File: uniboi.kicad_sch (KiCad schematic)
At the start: 0 parts

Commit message: WIP: first draft of schematics
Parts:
- added C1: 4.7uF, symbol Device:C
- added C2, C3: 0.1uF, symbol Device:C
- added C4, C6, C7: 1uF, symbol Device:C
- added C5: C, symbol Device:C
- added F1: 1A, symbol Device:Polyfuse
- added J1: USB_C_Receptacle_USB2.0_16P, symbol Connector:USB_C_Receptacle_USB2.0_16P
- added R1: 10k, symbol Device:R
- added R2, R3: 5.1k, symbol Device:R
- added SW1: SW_Push, symbol Switch:SW_Push
- added SW2: SW_SPDT, symbol Switch:SW_SPDT
- added U1: STM32G0B1CBTx, Package_QFP:LQFP-48_7x7mm_P0.5mm, symbol MCU_ST_STM32G0:STM32G0B1CBTx
- added U2: SRV05-4, Package_TO_SOT_SMD:SOT-23-6, symbol Power_Protection:SRV05-4
- added U3: XC6206P332MR, Package_TO_SOT_SMD:SOT-23-3, symbol Regulator_Linear:XC6206PxxxMR
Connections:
- new net: J1.B5 (CC2), R2.1
- new net: R1.2, SW2.2 (B)
- new net: J1.A5 (CC1), R3.1
- new net +3.3V: C1.1, C2.1, C3.1, C4.1, C7.1, SW2.3 (C), U1.4 (VBAT), U1.5 (VREF+), U1.6 (VDD), U3.2 (VO)
- new net +5V: C6.1, F1.2, U2.5 (VP), U3.3 (VI)
- new net BOOT0: R1.1, U1.36 (PA14)
- new net D+: J1.A6 (D+), J1.B6 (D+), U1.34 (PA10/PA12)
- new net D-: J1.A7 (D-), J1.B7 (D-), U1.33 (PA9/PA11)
- new net GND: C1.2, C2.2, C3.2, C4.2, C5.2, C6.2, C7.2, J1.A1 (GND), J1.A12 (GND), J1.B1 (GND), J1.B12 (GND), J1.S1 (SHIELD), R2.2, R3.2, SW1.2, SW2.1 (A), U1.7 (VSS), U2.2 (VN), U3.1 (GND)
- new net VBUS: F1.1, J1.A4 (VBUS), J1.A9 (VBUS), J1.B4 (VBUS), J1.B9 (VBUS)
- new net nRST: C5.1, SW1.1, U1.10 (PF2)
- no-connect marks 0 -> 2
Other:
- added sheet matrix (matrix.kicad_sch)

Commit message: added keyswitch footprint submodule
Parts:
- C1, C2, C3, C4, C5, C6, C7: footprint (none) -> Capacitor_SMD:C_0805_2012Metric
- F1: footprint (none) -> Fuse:Fuse_1206_3216Metric
- J1: footprint (none) -> Connector_USB:USB_C_Receptacle_HRO_TYPE-C-31-M-12
- R1, R2, R3: footprint (none) -> Resistor_SMD:R_0805_2012Metric
- SW1: footprint (none) -> Button_Switch_SMD:SW_SPST_TS-1088-xR020
- SW2: footprint (none) -> Button_Switch_SMD:SW_SPDT_PCM12
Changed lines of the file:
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@@
 			)
 		)
-		(property "Footprint" ""
+		(property "Footprint" "Capacitor_SMD:C_0805_2012Metric"
 			(at 350.2152 134.62 0)
 			(effects
@@
 			)
 		)
-		(property "Footprint" ""
+		(property "Footprint" "Resistor_SMD:R_0805_2012Metric"
 			(at 66.802 45.72 90)
 			(effects
@@
 			)
 		)
-		(property "Footprint" ""
+		(property "Footprint" "Capacitor_SMD:C_0805_2012Metric"
 			(at 195.2752 88.9 0)
 			(effects
@@
 			)
 		)
-		(property "Footprint" ""
+		(property "Footprint" "Capacitor_SMD:C_0805_2012Metric"
 			(at 180.0352 88.9 0)
 			(effects
@@
 			)
 		)
-		(property "Footprint" ""
+		(property "Footprint" "Button_Switch_SMD:SW_SPST_TS-1088-xR020"
 			(at 370.84 130.81 0)
 			(effects
@@
 			)
 		)
-		(property "Footprint" ""
+		(property "Footprint" "Button_Switch_SMD:SW_SPDT_PCM12"
 			(at 370.84 157.48 0)
 			(effects
@@
 			)
 		)
-		(property "Footprint" ""
+		(property "Footprint" "Capacitor_SMD:C_0805_2012Metric"
 			(at 237.1852 83.82 0)
 			(effects
@@
 			)
 		)
-		(property "Footprint" ""
+		(property "Footprint" "Resistor_SMD:R_0805_2012Metric"
 			(at 359.41 159.258 90)
 			(effects
@@
 			)
 		)
-		(property "Footprint" ""
+		(property "Footprint" "Connector_USB:USB_C_Receptacle_HRO_TYPE-C-31-M-12"
 			(at 36.83 48.26 0)
 			(effects
@@
 			)
 		)
-		(property "Footprint" ""
+		(property "Footprint" "Capacitor_SMD:C_0805_2012Metric"
 			(at 129.2352 45.72 0)
 			(effects
@@
 			)
 		)
-		(property "Footprint" ""
+		(property "Footprint" "Capacitor_SMD:C_0805_2012Metric"
 			(at 101.2952 45.72 0)
 			(effects
@@
 			)
 		)
-		(property "Footprint" ""
+		(property "Footprint" "Fuse:Fuse_1206_3216Metric"
 			(at 72.39 31.75 0)
 			(effects
@@
 			)
 		)
-		(property "Footprint" ""
+		(property "Footprint" "Capacitor_SMD:C_0805_2012Metric"
 			(at 249.8852 83.82 0)
 			(effects
@@
 			)
 		)
-		(property "Footprint" ""
+		(property "Footprint" "Resistor_SMD:R_0805_2012Metric"
 			(at 75.692 45.72 90)
 			(effects

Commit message: WIP:routing
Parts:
- C1, C2, C3, C4, C6, C7: footprint Capacitor_SMD:C_0805_2012Metric -> Capacitor_SMD:C_0402_1005Metric
- C5: value C -> 0.1uF; footprint Capacitor_SMD:C_0805_2012Metric -> Capacitor_SMD:C_0402_1005Metric
- R1, R2, R3: footprint Resistor_SMD:R_0805_2012Metric -> Resistor_SMD:R_0402_1005Metric
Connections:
- net COL1: now reaches U1.47 (PB8)
- net COL0: now reaches U1.48 (PB9)
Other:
- sheet matrix ports: added COL0, COL1, ROW0, ROW1; removed none
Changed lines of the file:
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@@
+		)
+	)
+	(global_label "COL1"
+		(shape input)
+		(at 151.13 123.19 0)
+		(fields_autoplaced yes)
+		(effects
+			(font
+				(size 1.27 1.27)
+			)
+			(justify left)
+		)
+		(property "Intersheetrefs" "${INTERSHEET_REFS}"
+			(at 158.9533 123.19 0)
+			(effects
+				(font
+					(size 1.27 1.27)
+				)
+				(justify left)
+				(hide yes)
+			)
 		)
 	)
@@
 		)
 	)
+	(global_label "COL0"
+		(shape input)
+		(at 151.13 119.38 0)
+		(fields_autoplaced yes)
+		(effects
+			(font
+				(size 1.27 1.27)
+			)
+			(justify left)
+		)
+		(property "Intersheetrefs" "${INTERSHEET_REFS}"
+			(at 158.9533 119.38 0)
+			(effects
+				(font
+					(size 1.27 1.27)
+				)
+				(justify left)
+				(hide yes)
+			)
+		)
+	)
 	(global_label "D+"
 		(shape input)
@@
 		)
 	)
+	(global_label "COL0"
+		(shape input)
+		(at 252.73 163.83 0)
+		(fields_autoplaced yes)
+		(effects
+			(font
+				(size 1.27 1.27)
+			)
+			(justify left)
+		)
+		(property "Intersheetrefs" "${INTERSHEET_REFS}"
+			(at 260.5533 163.83 0)
+			(effects
+				(font
+					(size 1.27 1.27)
+				)
+				(justify left)
+				(hide yes)
+			)
+		)
+	)
+	(global_label "COL1"
+		(shape input)
+		(at 252.73 161.29 0)
+		(fields_autoplaced yes)
+		(effects
+			(font
+				(size 1.27 1.27)
+			)
+			(justify left)
+		)
+		(property "Intersheetrefs" "${INTERSHEET_REFS}"
+			(at 260.5533 161.29 0)
+			(effects
+				(font
+					(size 1.27 1.27)
+				)
+				(justify left)
+				(hide yes)
+			)
+		)
+	)
 	(global_label "D-"
 		(shape input)
@@
 			)
 		)
-		(property "Value" "C"
+		(property "Value" "0.1uF"
 			(at 353.06 132.0799 0)
 			(effects
@@
 			)
 		)
-		(property "Footprint" "Capacitor_SMD:C_0805_2012Metric"
+		(property "Footprint" "Capacitor_SMD:C_0402_1005Metric"
 			(at 350.2152 134.62 0)
 			(effects
@@
 			)
 		)
-		(property "Footprint" "Resistor_SMD:R_0805_2012Metric"
+		(property "Footprint" "Resistor_SMD:R_0402_1005Metric"
 			(at 66.802 45.72 90)
 			(effects
@@
 			)
 		)
-		(property "Footprint" "Capacitor_SMD:C_0805_2012Metric"
+		(property "Footprint" "Capacitor_SMD:C_0402_1005Metric"
 			(at 195.2752 88.9 0)
 			(effects
@@
 			)
 		)
-		(property "Footprint" "Capacitor_SMD:C_0805_2012Metric"
+		(property "Footprint" "Capacitor_SMD:C_0402_1005Metric"
 			(at 180.0352 88.9 0)
 			(effects
@@
 			)
 		)
-		(property "Footprint" "Capacitor_SMD:C_0805_2012Metric"
+		(property "Footprint" "Capacitor_SMD:C_0402_1005Metric"
 			(at 237.1852 83.82 0)
 			(effects
@@
 			)
 		)
-		(property "Footprint" "Resistor_SMD:R_0805_2012Metric"
+		(property "Footprint" "Resistor_SMD:R_0402_1005Metric"
 			(at 359.41 159.258 90)
 			(effects
@@
 			)
 		)
-		(property "Footprint" "Capacitor_SMD:C_0805_2012Metric"
+		(property "Footprint" "Capacitor_SMD:C_0402_1005Metric"
 			(at 129.2352 45.72 0)
 			(effects
@@
 			)
 		)
-		(property "Footprint" "Capacitor_SMD:C_0805_2012Metric"
+		(property "Footprint" "Capacitor_SMD:C_0402_1005Metric"
 			(at 101.2952 45.72 0)
 			(effects
@@
 			)
 		)
-		(property "Footprint" "Capacitor_SMD:C_0805_2012Metric"
+		(property "Footprint" "Capacitor_SMD:C_0402_1005Metric"
 			(at 249.8852 83.82 0)
 			(effects
@@
 			)
 		)
-		(property "Footprint" "Resistor_SMD:R_0805_2012Metric"
+		(property "Footprint" "Resistor_SMD:R_0402_1005Metric"
 			(at 75.692 45.72 90)
 			(effects
@@
 	)
 	(sheet
-		(at 53.34 114.3)
-		(size 104.14 118.11)
+		(at 115.57 104.14)
+		(size 35.56 50.8)
 		(exclude_from_sim no)
 		(in_bom yes)
@@
 		)
 		(property "Sheetname" "matrix"
-			(at 53.34 113.5884 0)
+			(at 115.57 103.4284 0)
 			(effects
 				(font
@@
 		)
 		(property "Sheetfile" "matrix.kicad_sch"
-			(at 53.34 232.9946 0)
+			(at 115.57 155.5246 0)
 			(effects
 				(font
@@
 			)
 		)
+		(pin "COL1" input
+			(at 151.13 123.19 0)
+			(effects
+				(font
+					(size 1.27 1.27)
+				)
+				(justify right)
+			)
+		)
+		(pin "ROW1" input
+			(at 151.13 147.32 0)
+			(effects
+				(font
+					(size 1.27 1.27)
+				)
+				(justify right)
+			)
+		)
+		(pin "COL0" input
+			(at 151.13 119.38 0)
+			(effects
+				(font
+					(size 1.27 1.27)
+				)
+				(justify right)
+			)
+		)
+		(pin "ROW0" input
+			(at 151.13 143.51 0)
+			(effects
+				(font
+					(size 1.27 1.27)
+				)
+				(justify right)
+			)
+		)

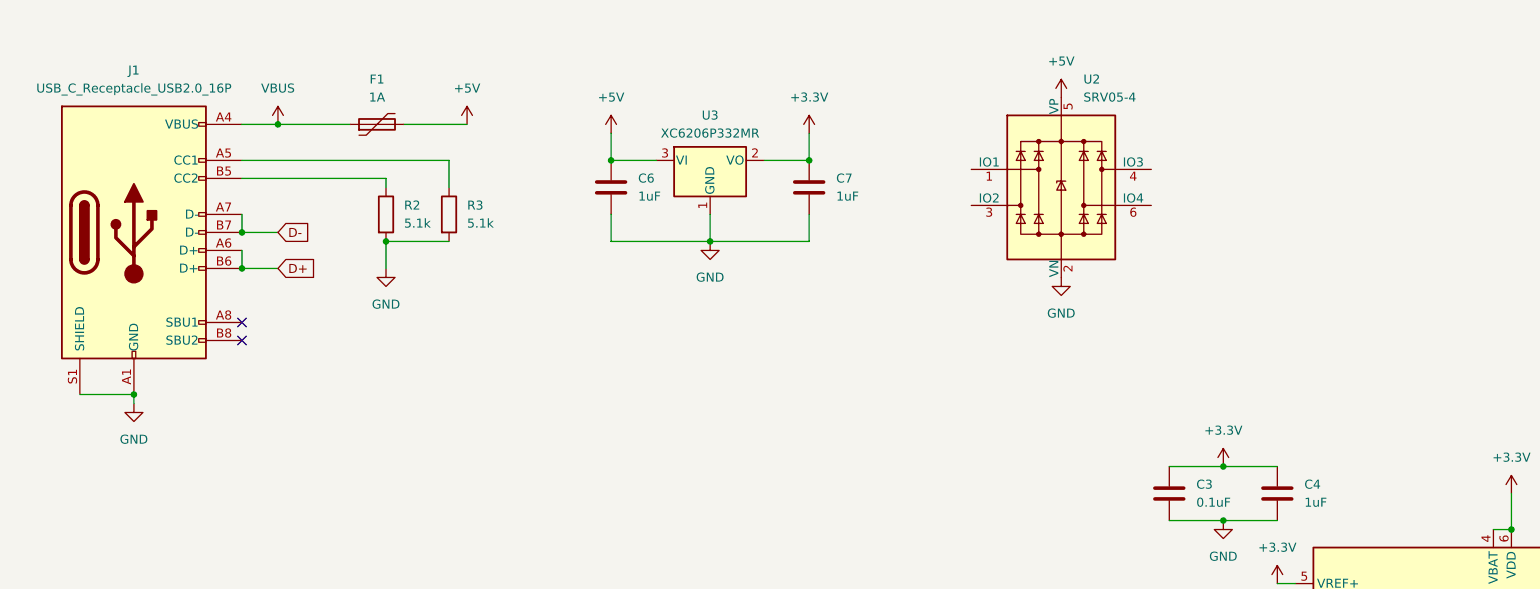
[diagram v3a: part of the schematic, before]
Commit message: WIP: changed usb-c connector, updated schematics with the SRV05-4, updated routing
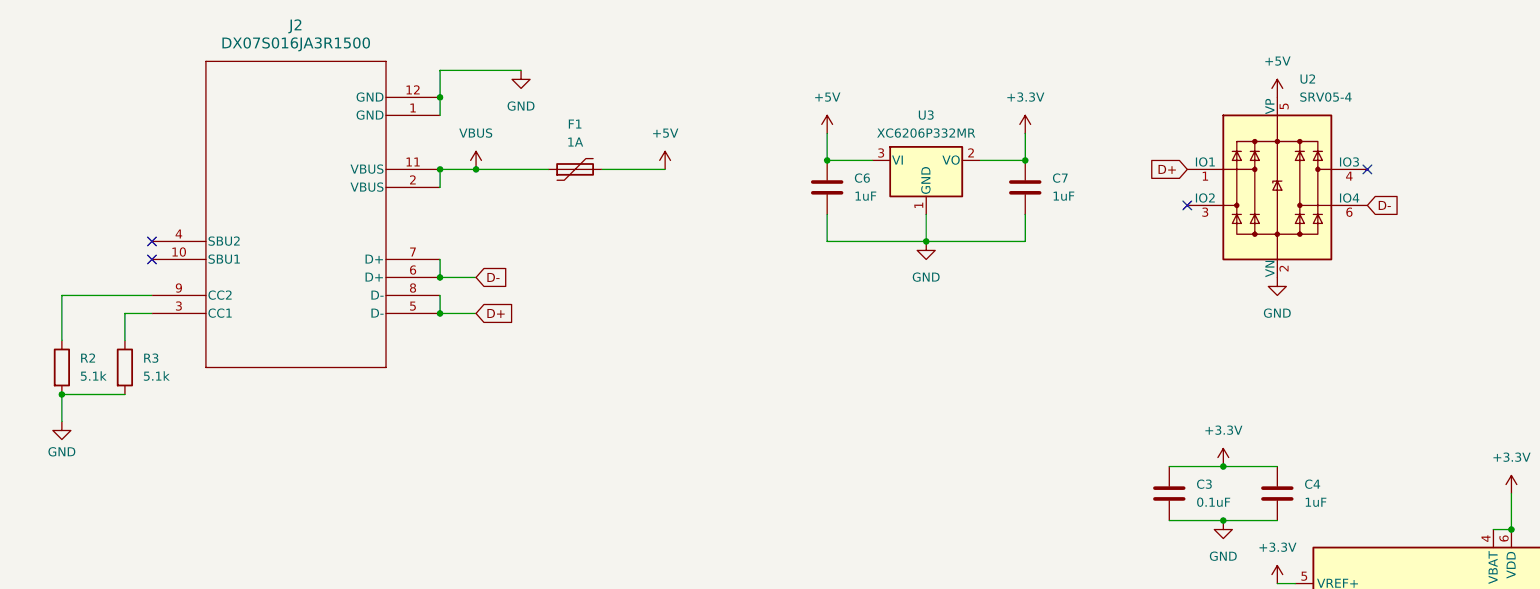
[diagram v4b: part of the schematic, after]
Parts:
- removed J1: USB_C_Receptacle_USB2.0_16P, Connector_USB:USB_C_Receptacle_HRO_TYPE-C-31-M-12, symbol Connector:USB_C_Receptacle_USB2.0_16P
- added J2: DX07S016JA3R1500, CONN12_DX07S_JAE, symbol USB_C_rmerli:DX07S016JA3R1500
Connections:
- net D+: now also U2.1 (IO1), J2.5 (D-), J2.8 (D-)
- net D-: now also U2.6 (IO4), J2.6 (D+), J2.7 (D+)
- net GND: now also J2.1 (GND), J2.12 (GND)
- net VBUS: now also J2.11 (VBUS), J2.2 (VBUS)
- net at R2.1: now also J2.9 (CC2)
- net at R3.1: now also J2.3 (CC1)
- no-connect marks 2 -> 4
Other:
- moved on the sheet: C6, C7, F1, R2, R3, U2, U3

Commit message: WIP: schematics and routing
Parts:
- renumbered C6 to C1, C7 to C2, C1 to C3, C2 to C4, C3 to C5, C4 to C6, C5 to C7, J2 to J1, R2 to R1, R3 to R2, R1 to R3, U3 to U1, U1 to U3
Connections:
- net D+: now also U2.4 (IO3); no longer U2.1 (IO1)
- net D-: now also U2.3 (IO2); no longer U2.6 (IO4)
- net CC1: now reaches J1.3 (CC1), R2.1
- net CC2: now reaches J1.9 (CC2), R1.1

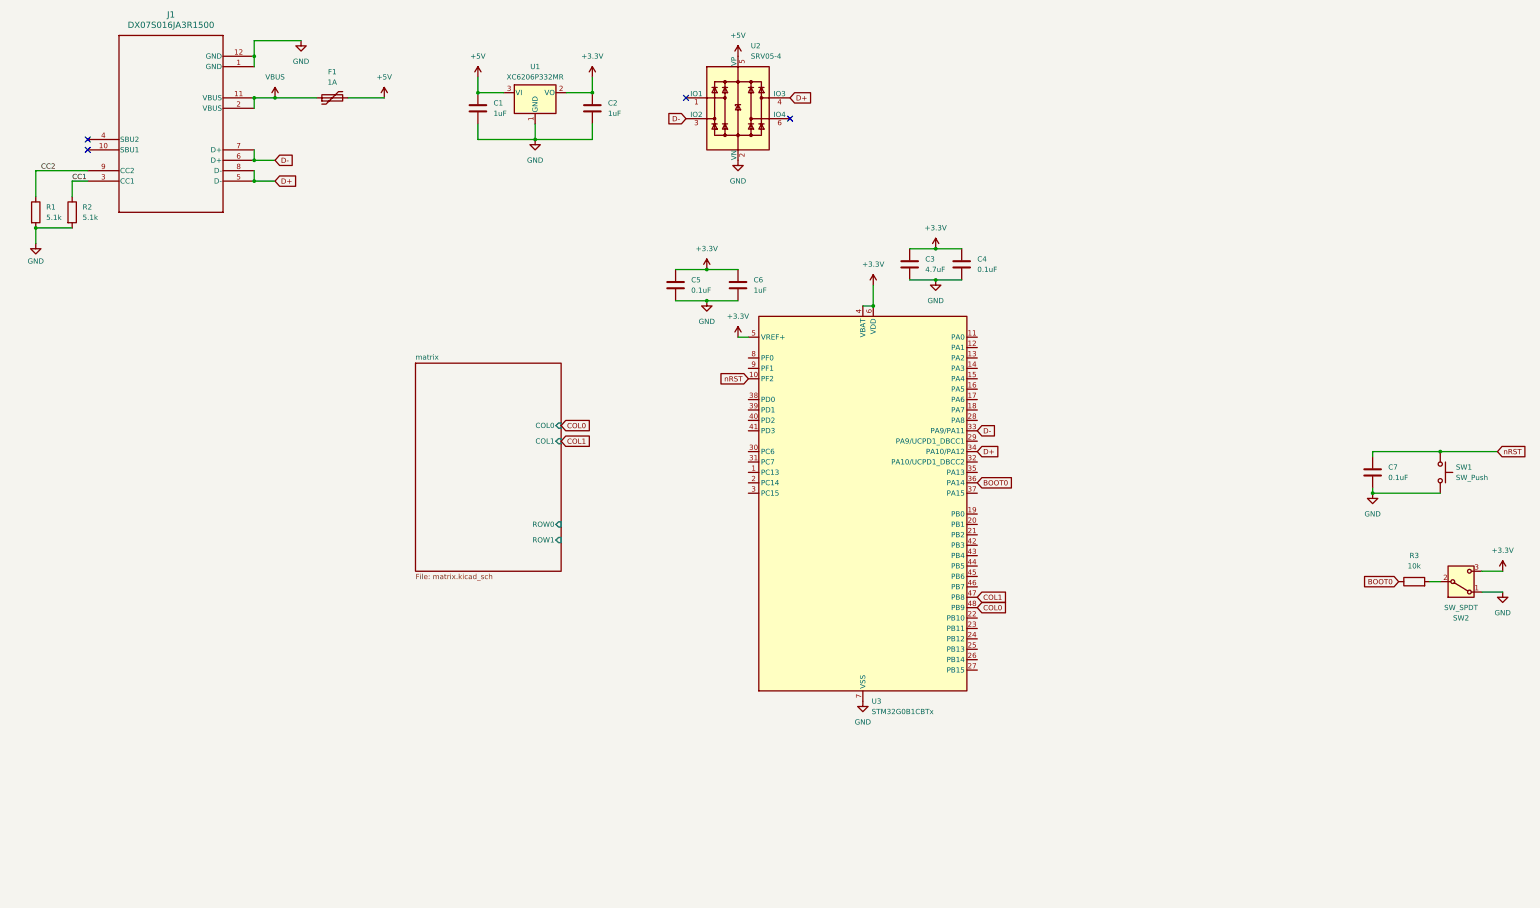
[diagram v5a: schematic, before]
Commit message: WIP: routed matrix and added swdio
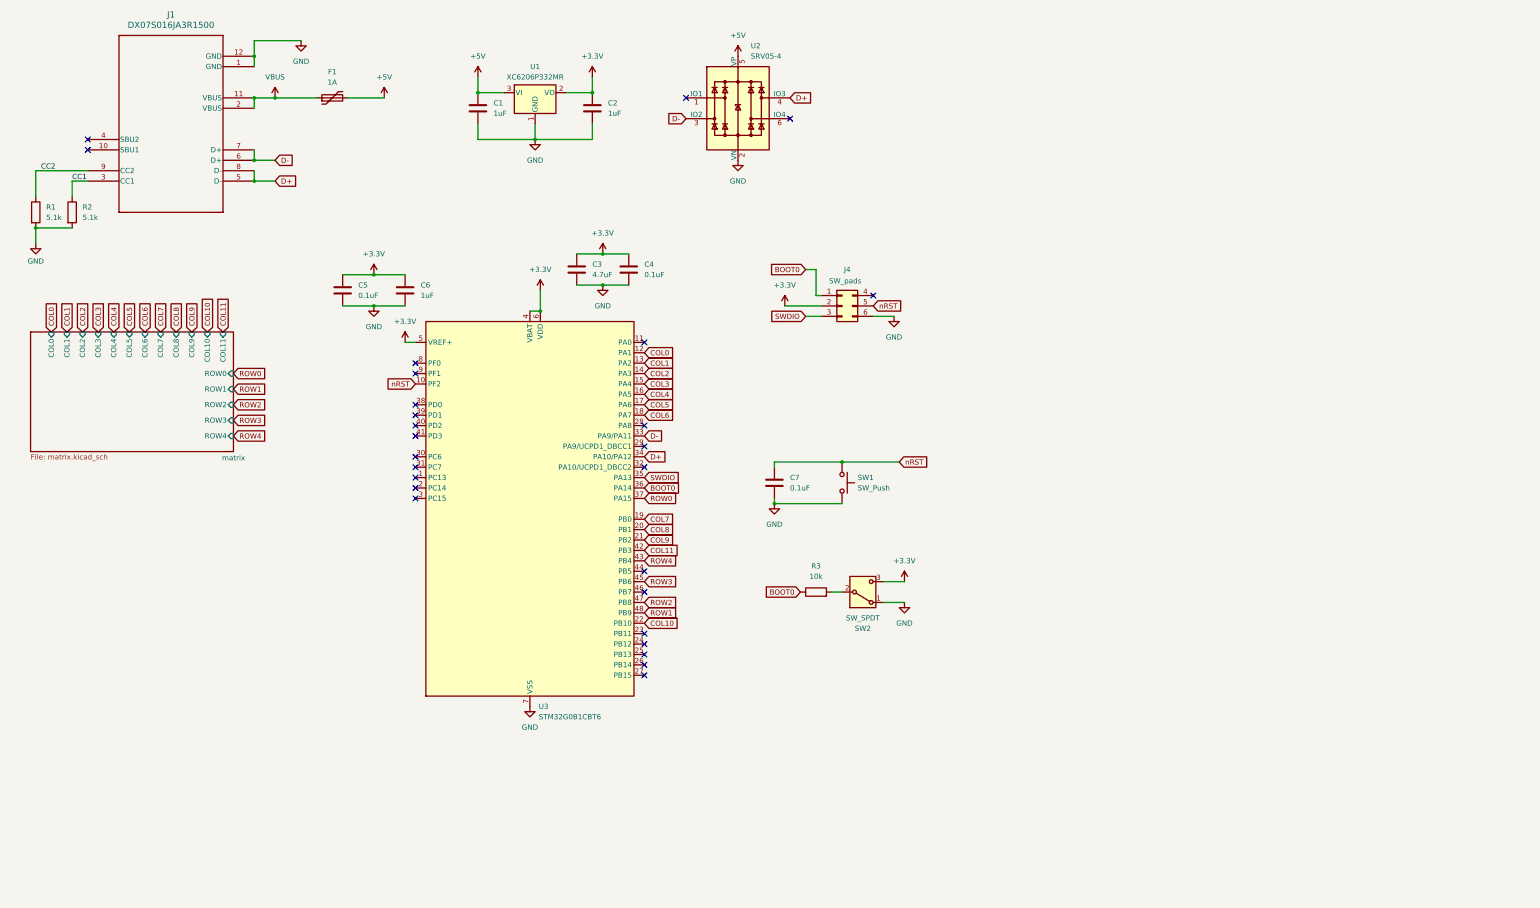
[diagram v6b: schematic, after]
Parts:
- added J4: SW_pads, Connector:Tag-Connect_TC2030-IDC-NL_2x03_P1.27mm_Vertical, symbol Connector_Generic:Conn_02x03_Top_Bottom
- J1: footprint CONN12_DX07S_JAE -> USB_C_rmerli:CONN12_DX07S_JAE_no_edge_cuts
- U3: value STM32G0B1CBTx -> STM32G0B1CBT6
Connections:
- net +3.3V: now also J4.2 (Pin_2)
- net BOOT0: now also J4.1 (Pin_1)
- net COL0: now also U3.12 (PA1); no longer U3.48 (PB9)
- net COL1: now also U3.13 (PA2); no longer U3.47 (PB8)
- net GND: now also J4.6 (Pin_6)
- net nRST: now also J4.5 (Pin_5)
- net COL2: now reaches U3.14 (PA3)
- net COL3: now reaches U3.15 (PA4)
- net COL4: now reaches U3.16 (PA5)
- net COL5: now reaches U3.17 (PA6)
- net COL6: now reaches U3.18 (PA7)
- net COL7: now reaches U3.19 (PB0)
- net COL8: now reaches U3.20 (PB1)
- net COL9: now reaches U3.21 (PB2)
- net COL10: now reaches U3.22 (PB10)
- net SWDIO: now reaches U3.35 (PA13)
- net SWDIO: now also J4.3 (Pin_3)
- net ROW0: now reaches U3.37 (PA15)
- net COL11: now reaches U3.42 (PB3)
- net ROW4: now reaches U3.43 (PB4)
- net ROW3: now reaches U3.45 (PB6)
- new net ROW1: U3.48 (PB9)
- new net ROW2: U3.47 (PB8)
- no-connect marks 4 -> 27
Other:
- sheet matrix ports: added COL10, COL11, COL2, COL3, COL4, COL5, COL6, COL7, COL8, COL9, ROW2, ROW3, ROW4; removed none
- moved on the sheet: C3, C4, C5, C6, C7, R3, SW1, SW2, U3

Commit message: clean up and final touches
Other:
- note added: "Bootsel - reset"
- note added: "ESD protection"
- note added: "Key Matrix"
- note added: "MCU"
- note added: "SW"
- note added: "USB - POWER"
- moved on the sheet: C1, C2, C3, C4, C5, C6, C7, F1, J1, J4, R1, R2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
